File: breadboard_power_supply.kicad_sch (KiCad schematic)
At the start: 18 parts, among them J1 Barrel_Jack_Switch, J11 Conn_01x07, J13 PJ-063AH, J4 Screw_Terminal_01x02, J6 Conn_01x03_Male, J7 Screw_Terminal_01x02, U1 LM7805_TO220 (1A), U2 LM317_TO-220 (1,5A)

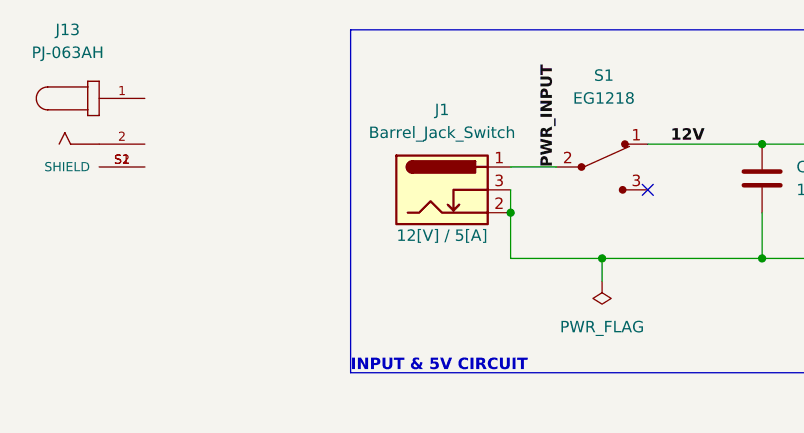
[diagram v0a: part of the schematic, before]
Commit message: Clear separation of 2 designs : with usb
consumption calculation , manuals / issue with slider switch to be checked if ok
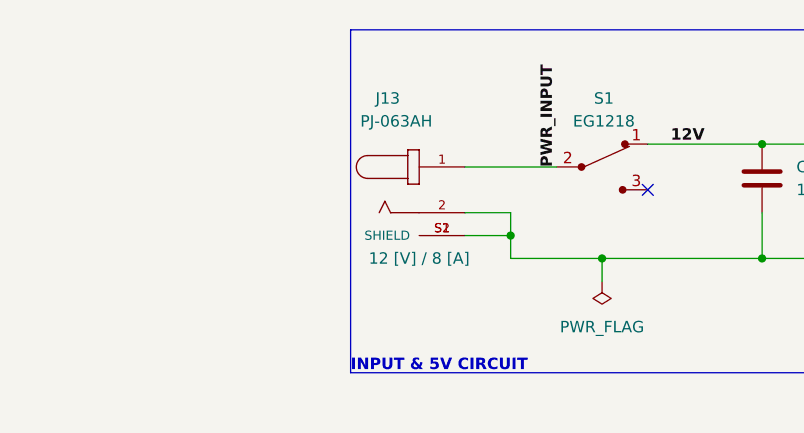
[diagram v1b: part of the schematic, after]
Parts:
- removed J1: Barrel_Jack_Switch, PJ-059AH:CUI_PJ-059AH, symbol Connector:Barrel_Jack_Switch
- J13: M.DIMENSIONS (none) -> 2.0 x 6.5 [mm]; PWR_SUP_EXAMPLE (none) -> https://www.amazon.de/DUMVOIN-Netzteiladapter-Spannungswand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; RATED_SUPPLY (none) -> 12 [V] / 8 [A]
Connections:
- net GND: now also J13.2, J13.S1 (SHIELD), J13.S2 (SHIELD)
- net PWR_INPUT: now also J13.1
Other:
- moved on the sheet: J13
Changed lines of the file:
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@@
   (junction (at 104.14 116.84) (diameter 0) (color 0 0 0 0)
   )
+  (junction (at 76.2 55.88) (diameter 0) (color 0 0 0 0)
+  )
   (junction (at 124.46 58.42) (diameter 0) (color 0 0 0 0)
   )
@@
   )
   (junction (at 71.12 96.52) (diameter 0) (color 0 0 0 0)
-  )
-  (junction (at 76.2 53.34) (diameter 0) (color 0 0 0 0)
   )
   (junction (at 104.14 45.72) (diameter 0) (color 0 0 0 0)
@@
     (stroke (width 0) (type default) (color 0 0 0 0))
   )
+  (wire (pts (xy 76.2 53.34) (xy 76.2 55.88))
+    (stroke (width 0) (type default) (color 0 0 0 0))
+  )
   (wire (pts (xy 114.3 96.52) (xy 119.38 96.52))
     (stroke (width 0) (type default) (color 0 0 0 0))
@@
     (stroke (width 0) (type default) (color 0 0 0 0))
   )
-  (wire (pts (xy 76.2 48.26) (xy 81.28 48.26))
+  (wire (pts (xy 71.12 48.26) (xy 81.28 48.26))
     (stroke (width 0) (type default) (color 0 0 0 0))
   )
@@
     (stroke (width 0) (type default) (color 0 0 0 0))
   )
-  (wire (pts (xy 76.2 53.34) (xy 76.2 58.42))
-    (stroke (width 0) (type default) (color 0 0 0 0))
-  )
   (wire (pts (xy 86.36 58.42) (xy 86.36 60.96))
     (stroke (width 0) (type default) (color 0 0 0 0))
@@
     (stroke (width 0) (type default) (color 0 0 0 0))
   )
-  (wire (pts (xy 76.2 50.8) (xy 76.2 53.34))
+  (wire (pts (xy 71.12 53.34) (xy 76.2 53.34))
+    (stroke (width 0) (type default) (color 0 0 0 0))
+  )
+  (wire (pts (xy 71.12 55.88) (xy 76.2 55.88))
     (stroke (width 0) (type default) (color 0 0 0 0))
   )
@@
   )
   (polyline (pts (xy 175.26 132.08) (xy 175.26 162.56))
+    (stroke (width 0) (type default) (color 0 0 0 0))
+  )
+  (wire (pts (xy 76.2 55.88) (xy 76.2 58.42))
     (stroke (width 0) (type default) (color 0 0 0 0))
   )
@@
   (symbol (lib_id "digkey_slide_switch:EG1218") (at 86.36 48.26 0) (unit 1)
     (in_bom yes) (on_board yes) (fields_autoplaced)
-    (property "Reference" "S1" (id 0) (at 86.5632 38.1 0))
-    (property "Value" "EG1218" (id 1) (at 86.5632 40.64 0))
+    (property "Reference" "S1" (id 0) (at 86.5632 40.64 0))
+    (property "Value" "EG1218" (id 1) (at 86.5632 43.18 0))
     (property "Footprint" "digkey_slide_switch:Switch_Slide_11.6x4mm_EG1218" (id 2) (at 86.5632 43.18 0)
       (effects (font (size 1.27 1.27)) hide)
@@
     (pin "2")
   )
-  (symbol (lib_id "PJ-063AH:PJ-063AH") (at 30.48 43.18 0) (unit 1)
-    (in_bom yes) (on_board yes) (fields_autoplaced)
-    (property "Reference" "J13" (id 0) (at 26.9875 33.02 0))
-    (property "Value" "PJ-063AH" (id 1) (at 26.9875 35.56 0))
-    (property "Footprint" "Connector_BarrelJack:BarrelJack_CUI_PJ-063AH_Horizontal" (id 2) (at 30.48 43.18 0)
+  (symbol (lib_id "PJ-063AH:PJ-063AH") (at 66.04 50.8 0) (unit 1)
+    (in_bom yes) (on_board yes)
+    (property "Reference" "J13" (id 0) (at 62.5475 40.64 0))
+    (property "Value" "PJ-063AH" (id 1) (at 63.5 43.18 0))
+    (property "Footprint" "Connector_BarrelJack:BarrelJack_CUI_PJ-063AH_Horizontal" (id 2) (at 66.04 50.8 0)
       (effects (font (size 1.27 1.27)) (justify left bottom) hide)
     )
-    (property "Datasheet" "" (id 3) (at 30.48 43.18 0)
+    (property "Datasheet" "https://www.mouser.de/datasheet/2/670/pj_063ah-1778660.pdf" (id 3) (at 66.04 50.8 0)
       (effects (font (size 1.27 1.27)) (justify left bottom) hide)
     )
-    (property "PARTREV" "1.02" (id 4) (at 30.48 43.18 0)
+    (property "PARTREV" "1.02" (id 4) (at 66.04 50.8 0)
       (effects (font (size 1.27 1.27)) (justify left bottom) hide)
     )
-    (property "MANUFACTURER" "CUI INC" (id 5) (at 30.48 43.18 0)
+    (property "MANUFACTURER" "CUI INC" (id 5) (at 66.04 50.8 0)
       (effects (font (size 1.27 1.27)) (justify left bottom) hide)
     )
-    (property "STANDARD" "Manufacturer recommendations" (id 6) (at 30.48 43.18 0)
+    (property "STANDARD" "Manufacturer recommendations" (id 6) (at 66.04 50.8 0)
       (effects (font (size 1.27 1.27)) (justify left bottom) hide)
+    )
+    (property "RATED_SUPPLY" "12 [V] / 8 [A]" (id 7) (at 66.04 58.42 0))
+    (property "M.DIMENSIONS" "2.0 x 6.5 [mm]" (id 8) (at 66.04 50.8 0)
+      (effects (font (size 1.27 1.27)) hide)
+    )
+    (property "PWR_SUP_EXAMPLE" "https://www.amazon.de/DUMVOIN-Netzteiladapter-Spannungswandler-Flexible-LED-Streifen-Lichter/dp/B075S24G5B" (id 9) (at 66.04 50.8 0)
+      (effects (font (size 1.27 1.27)) hide)
     )
     (pin "1")
@@
     (pin "3")
   )
-  (symbol (lib_id "Connector:Barrel_Jack_Switch") (at 68.58 50.8 0) (unit 1)
-    (in_bom yes) (on_board yes)
-    (property "Reference" "J1" (id 0) (at 68.58 41.91 0))
-    (property "Value" "Barrel_Jack_Switch" (id 1) (at 68.58 44.45 0))
-    (property "Footprint" "PJ-059AH:CUI_PJ-059AH" (id 2) (at 69.85 51.816 0)
-      (effects (font (size 1.27 1.27)) hide)
-    )
-    (property "Datasheet" "~" (id 3) (at 69.85 51.816 0)
-      (effects (font (size 1.27 1.27)) hide)
-    )
-    (property "PI_PLUG" "https://www.amazon.com/HitLights-Transformer-UL-Listed-Lighting-Adapter/dp/B007ME2HMQ/ref=sr_1_1_sspa?keywords=12v+dc+plug&qid=1653777105&sr=8-1-spons&psc=1&spLa=ZW5jcnlwdGVkUXVhbGlmaWVyPUFSWDBMWlFIOEk0SlgmZW5jcnlwdGVkSWQ9QTAzNTIwNzEyUTYzMFFHNTJEQjAzJmVuY3J5cHRlZEFkSWQ9QTAyOTk3ODIxR1JHUDE2MzlJRzU0JndpZGdldE5hbWU9c3BfYXRmJmFjdGlvbj1jbGlja1JlZGlyZWN0JmRvTm90TG9nQ2xpY2s9dHJ1ZQ==" (id 4) (at 68.58 50.8 0)
-      (effects (font (size 1.27 1.27)) hide)
-    )
-    (property "SUGGESTED" "12[V] / 5[A]" (id 5) (at 68.58 55.88 0))
-    (property "PWR_SUPP" "https://www.cableworks.gr/ilektronika/power-supply/oem/12v-3a-dc-power-supply-with-barrel-jack/" (id 6) (at 68.58 50.8 0)
-      (effects (font (size 1.27 1.27)) hide)
-    )
-    (property "ALTERNATIVE_PWR_SUP" "https://www.beegadget.gr/index.php?route=product%2Fproduct&product_id=21497&ref=bestprice.gr" (id 7) (at 68.58 50.8 0)
-      (effects (font (size 1.27 1.27)) hide)
-    )
-    (property "M. DIMENSIONS" "2.0 x 5.5 [mm]" (id 8) (at 68.58 50.8 0)
-      (effects (font (size 1.27 1.27)) hide)
-    )
-    (pin "1")
-    (pin "2")
-    (pin "3")
-  )
   (symbol (lib_id "power:GND") (at 203.2 60.96 270) (unit 1)
     (in_bom yes) (on_board yes) (fields_autoplaced)
@@
       (reference "D1") (unit 1) (value "LED") (footprint "LED_SMD:LED_0805_2012Metric")
     )
-    (path "/b59d3927-1cf4-41ca-91f5-3c44dbcc526e"
-      (reference "J1") (unit 1) (value "Barrel_Jack_Switch") (footprint "PJ-059AH:CUI_PJ-059AH")
-    )
     (path "/3c44e781-1190-4e9e-8bbc-c825cbc80c09/32088f69-5ea6-45d7-aabd-4f46838450c7"

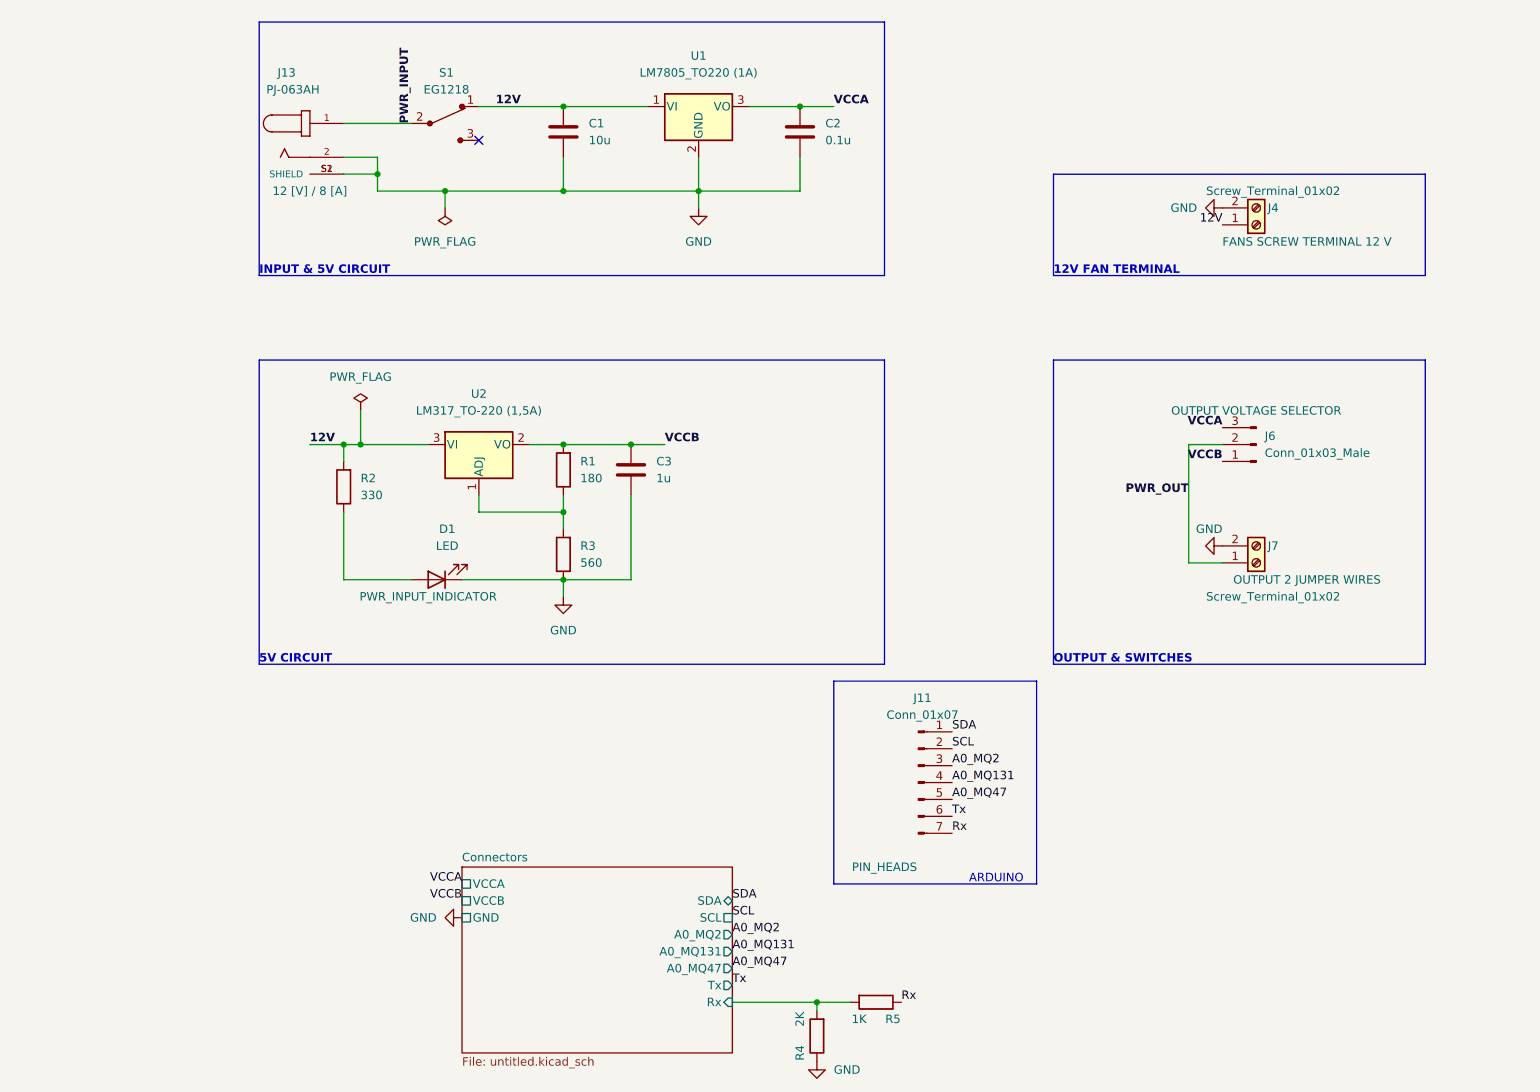
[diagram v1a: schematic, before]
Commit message: Design Rectified
Added pinheads & -sockets, all components and parts with their datasheets , power calculations and details - design improvement route tracks thickness check and calculation & F. silkscreening. Remaining : route tracks on the pcb
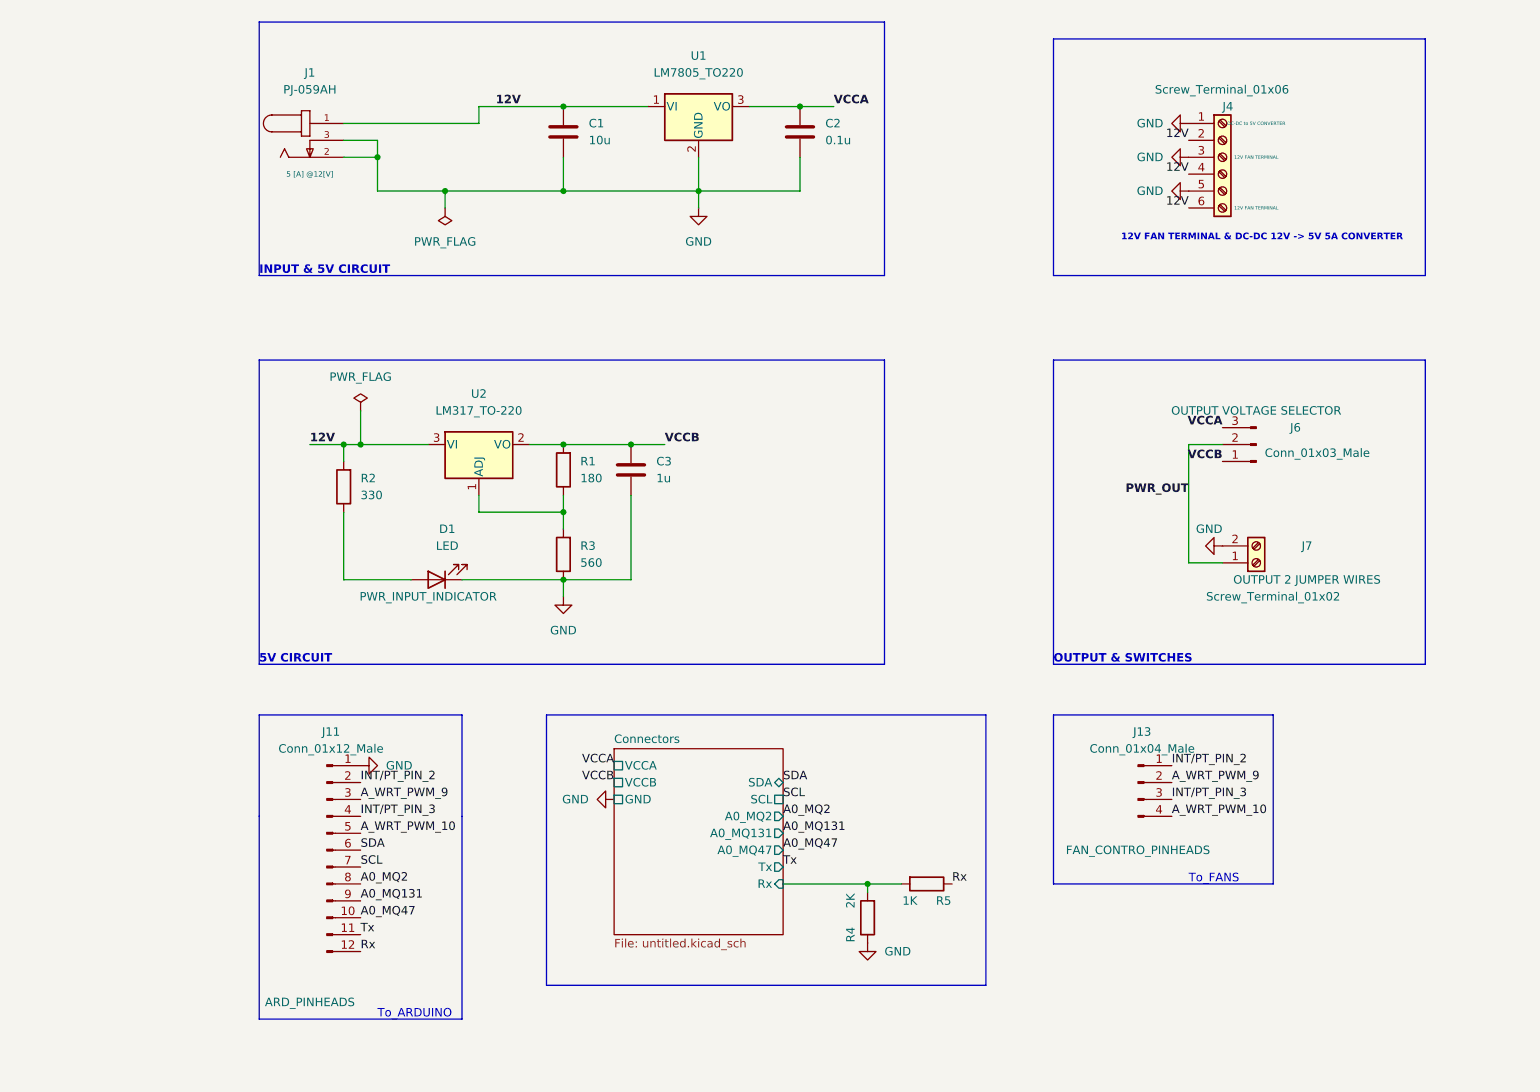
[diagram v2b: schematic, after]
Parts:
- removed J11: Conn_01x07, Connector_PinSocket_2.54mm:PinSocket_1x07_P2.54mm_Vertical, symbol Connector:Conn_01x07_Male
- removed J13: PJ-063AH, Connector_BarrelJack:BarrelJack_CUI_PJ-063AH_Horizontal, symbol PJ-063AH:PJ-063AH
- removed J4: Screw_Terminal_01x02, TerminalBlock:TerminalBlock_bornier-2_P5.08mm, symbol Connector:Screw_Terminal_01x02
- removed S1: EG1218, digkey_slide_switch:Switch_Slide_11.6x4mm_EG1218, symbol digkey_slide_switch:EG1218
- added J1: PJ-059AH, PJ-059AH:CUI_PJ-059AH, symbol PJ-059AH:PJ-059AH
- added J11: Conn_01x12_Male, Connector_PinSocket_2.54mm:PinSocket_1x12_P2.54mm_Vertical, symbol Connector:Conn_01x12_Male
- added J13: Conn_01x04_Male, Connector_PinSocket_2.54mm:PinSocket_1x04_P2.54mm_Vertical, symbol Connector:Conn_01x04_Male
- added J4: Screw_Terminal_01x06, TerminalBlock:TerminalBlock_bornier-6_P5.08mm, symbol Connector:Screw_Terminal_01x06
- J7: Rating (none) -> 8 [A]; Type (none) -> CTBP0508
- U1: value LM7805_TO220 (1A) -> LM7805_TO220; Rating (none) -> 1 [A]
- U2: value LM317_TO-220 (1,5A) -> LM317_TO-220; Rating (none) -> 1,5 [A]
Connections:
- net 12V: now also J1.1, J4.2 (Pin_2), J4.4 (Pin_4), J4.6 (Pin_6)
- net A0_MQ131: now also J11.9 (Pin_9)
- net A0_MQ2: now also J11.8 (Pin_8)
- net A0_MQ47: now also J11.10 (Pin_10)
- net GND: now also J1.2, J1.3, J11.1 (Pin_1), J4.1 (Pin_1), J4.3 (Pin_3), J4.5 (Pin_5)
- net Rx: now also J11.12 (Pin_12)
- net SCL: now also J11.7 (Pin_7)
- net SDA: now also J11.6 (Pin_6)
- net Tx: now also J11.11 (Pin_11)
- new net A_WRT_PWM_10: J11.5 (Pin_5), J13.4 (Pin_4)
- new net A_WRT_PWM_9: J11.3 (Pin_3), J13.2 (Pin_2)
- new net INT/PT_PIN_2: J11.2 (Pin_2), J13.1 (Pin_1)
- new net INT/PT_PIN_3: J11.4 (Pin_4), J13.3 (Pin_3)
- no-connect marks 1 -> 0
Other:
- note added: "12V FAN TERMINAL & DC-DC 12V -> 5V 5A CONVERTER"
- note added: "Το_ARDUINO"
- note added: "Το_FANS"
- note removed: "12V FAN TERMINAL"
- note removed: "ARDUINO"
- moved on the sheet: R4, R5
